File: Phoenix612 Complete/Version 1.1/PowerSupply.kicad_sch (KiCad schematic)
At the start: 20 parts, among them J2 PWR, J3 uC PTT, K1 G5V-2, Q1 2N3904, U3 LM7805

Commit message: Update 9Mar23
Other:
- moved on the sheet: C10
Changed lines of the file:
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@@
     (stroke (width 0) (type default) (color 0 0 0 0))
   )
-  (wire (pts (xy 51.435 102.235) (xy 51.435 103.505))
+  (wire (pts (xy 51.435 102.235) (xy 51.435 104.14))
     (stroke (width 0) (type default) (color 0 0 0 0))
   )
@@
     (stroke (width 0) (type default) (color 0 0 0 0))
   )
-  (wire (pts (xy 51.435 111.125) (xy 51.435 114.935))
+  (wire (pts (xy 51.435 111.76) (xy 51.435 114.935))
     (stroke (width 0) (type default) (color 0 0 0 0))
   )
@@
     (pin "2")
   )
-  (symbol (lib_id "Device:C_Polarized") (at 51.435 107.315 0) (unit 1)
-    (in_bom yes) (on_board yes) (fields_autoplaced)
-    (property "Reference" "C10" (id 0) (at 54.61 105.1559 0)
+  (symbol (lib_id "Device:C_Polarized") (at 51.435 107.95 0) (unit 1)
+    (in_bom yes) (on_board yes) (fields_autoplaced)
+    (property "Reference" "C10" (id 0) (at 54.61 105.7909 0)
       (effects (font (size 1.27 1.27)) (justify left))
     )
-    (property "Value" "22u" (id 1) (at 54.61 107.6959 0)
+    (property "Value" "22u" (id 1) (at 54.61 108.3309 0)
       (effects (font (size 1.27 1.27)) (justify left))
     )
-    (property "Footprint" "Capacitor_THT:CP_Radial_D8.0mm_P2.50mm" (id 2) (at 52.4002 111.125 0)
-      (effects (font (size 1.27 1.27)) hide)
-    )
-    (property "Datasheet" "~" (id 3) (at 51.435 107.315 0)
-      (effects (font (size 1.27 1.27)) hide)
-    )
+    (property "Footprint" "Capacitor_THT:CP_Radial_D8.0mm_P2.50mm" (id 2) (at 52.4002 111.76 0)
+      (effects (font (size 1.27 1.27)) hide)
+    )
+    (property "Datasheet" "~" (id 3) (at 51.435 107.95 0)
+      (effects (font (size 1.27 1.27)) hide)
+    )

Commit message: Update_17Mar23
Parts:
- added J51: VCC, Connector_BarrelJack:BarrelJack_GCT_DCJ200-10-A_Horizontal, symbol Connector:Barrel_Jack
- D1: value 1N4001 -> 1N5817; symbol Diode:1N4001 -> Diode:1N5817
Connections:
- net GND: now also J51.2
- net VCC: now reaches D1.2 (A), J2.2 (Pin_2)
- net VCC: now also J51.1
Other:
- moved on the sheet: D1, D2, D3, D4, R11, R12, R13

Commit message: Update 17Mar23
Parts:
- renumbered J2 to J3, J51 to J4, J3 to J5
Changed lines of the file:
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@@
   (symbol (lib_id "power:GND") (at 177.165 80.645 0) (unit 1)
     (in_bom yes) (on_board yes) (fields_autoplaced)
-    (property "Reference" "#PWR011" (id 0) (at 177.165 86.995 0)
+    (property "Reference" "#PWR022" (id 0) (at 177.165 86.995 0)
       (effects (font (size 1.27 1.27)) hide)
     )
@@
   (symbol (lib_id "Connector_Generic:Conn_01x03") (at 93.345 53.975 0) (unit 1)
     (in_bom yes) (on_board yes) (fields_autoplaced)
-    (property "Reference" "J2" (id 0) (at 96.52 52.7049 0)
+    (property "Reference" "J3" (id 0) (at 96.52 52.7049 0)
       (effects (font (size 1.27 1.27)) (justify left))
     )
@@
   (symbol (lib_id "Connector:Barrel_Jack") (at 55.245 55.245 0) (unit 1)
     (in_bom yes) (on_board yes) (fields_autoplaced)
-    (property "Reference" "J51" (id 0) (at 55.245 45.72 0))
+    (property "Reference" "J4" (id 0) (at 55.245 45.72 0))
     (property "Value" "VCC" (id 1) (at 55.245 48.26 0))
     (property "Footprint" "Connector_BarrelJack:BarrelJack_GCT_DCJ200-10-A_Horizontal" (id 2) (at 56.515 56.261 0)
@@
   (symbol (lib_id "power:PWR_FLAG") (at 78.105 33.02 180) (unit 1)
     (in_bom yes) (on_board yes)
-    (property "Reference" "#FLG016" (id 0) (at 78.105 34.925 0)
+    (property "Reference" "#FLG06" (id 0) (at 78.105 34.925 0)
       (effects (font (size 1.27 1.27)) hide)
     )
@@
   (symbol (lib_id "power:GND") (at 102.235 151.765 0) (unit 1)
     (in_bom yes) (on_board yes) (fields_autoplaced)
-    (property "Reference" "#PWR015" (id 0) (at 102.235 158.115 0)
+    (property "Reference" "#PWR026" (id 0) (at 102.235 158.115 0)
       (effects (font (size 1.27 1.27)) hide)
     )
@@
   (symbol (lib_id "power:GND") (at 33.655 32.385 0) (unit 1)
     (in_bom yes) (on_board yes) (fields_autoplaced)
-    (property "Reference" "#PWR09" (id 0) (at 33.655 38.735 0)
+    (property "Reference" "#PWR019" (id 0) (at 33.655 38.735 0)
       (effects (font (size 1.27 1.27)) hide)
     )
@@
   (symbol (lib_id "power:GND") (at 116.205 171.45 0) (unit 1)
     (in_bom yes) (on_board yes)
-    (property "Reference" "#PWR017" (id 0) (at 116.205 177.8 0)
+    (property "Reference" "#PWR028" (id 0) (at 116.205 177.8 0)
       (effects (font (size 1.27 1.27)) hide)
     )
@@
   (symbol (lib_id "power:GND") (at 66.675 57.785 0) (unit 1)
     (in_bom yes) (on_board yes) (fields_autoplaced)
-    (property "Reference" "#PWR010" (id 0) (at 66.675 64.135 0)
+    (property "Reference" "#PWR020" (id 0) (at 66.675 64.135 0)
       (effects (font (size 1.27 1.27)) hide)
     )
@@
   (symbol (lib_id "Connector_Generic:Conn_01x02") (at 121.285 165.1 0) (unit 1)
     (in_bom yes) (on_board yes) (fields_autoplaced)
-    (property "Reference" "J3" (id 0) (at 124.46 165.0999 0)
+    (property "Reference" "J5" (id 0) (at 124.46 165.0999 0)
       (effects (font (size 1.27 1.27)) (justify left))
     )
@@
   (symbol (lib_id "power:GND") (at 198.12 80.645 0) (unit 1)
     (in_bom yes) (on_board yes) (fields_autoplaced)
-    (property "Reference" "#PWR013" (id 0) (at 198.12 86.995 0)
+    (property "Reference" "#PWR024" (id 0) (at 198.12 86.995 0)
       (effects (font (size 1.27 1.27)) hide)
     )
@@
   (symbol (lib_id "power:GND") (at 134.62 154.94 0) (unit 1)
     (in_bom yes) (on_board yes) (fields_autoplaced)
-    (property "Reference" "#PWR016" (id 0) (at 134.62 161.29 0)
+    (property "Reference" "#PWR027" (id 0) (at 134.62 161.29 0)
       (effects (font (size 1.27 1.27)) hide)
     )
@@
   (symbol (lib_id "power:GND") (at 67.945 118.745 0) (unit 1)
     (in_bom yes) (on_board yes) (fields_autoplaced)
-    (property "Reference" "#PWR014" (id 0) (at 67.945 125.095 0)
+    (property "Reference" "#PWR025" (id 0) (at 67.945 125.095 0)
       (effects (font (size 1.27 1.27)) hide)
     )
@@
   (symbol (lib_id "power:GND") (at 81.28 59.055 0) (unit 1)
     (in_bom yes) (on_board yes) (fields_autoplaced)
-    (property "Reference" "#PWR0112" (id 0) (at 81.28 65.405 0)
+    (property "Reference" "#PWR021" (id 0) (at 81.28 65.405 0)
       (effects (font (size 1.27 1.27)) hide)
     )
@@
   (symbol (lib_id "power:GND") (at 187.325 80.645 0) (unit 1)
     (in_bom yes) (on_board yes) (fields_autoplaced)
-    (property "Reference" "#PWR012" (id 0) (at 187.325 86.995 0)
-      (effects (font (size 1.27 1.27)) hide)
-    )
+    (property "Reference" "#PWR023" (id 0) (at 187.325 86.995 0)
+      (effects (font (size 1.27 1.27)) hide)
+    )

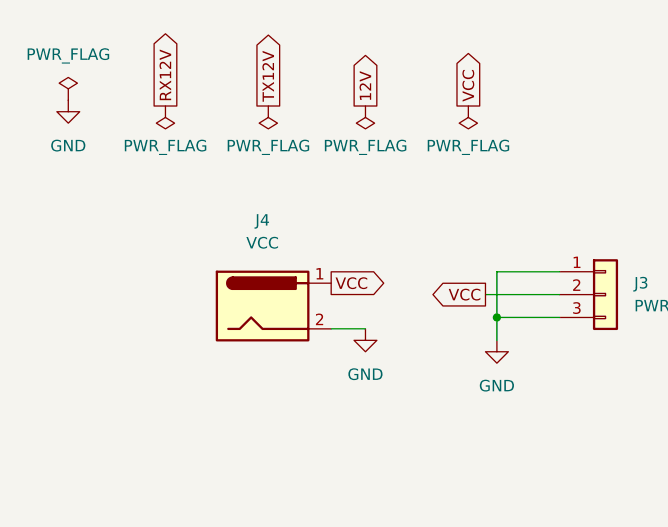
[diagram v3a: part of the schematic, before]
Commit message: Update LT1253 Tx
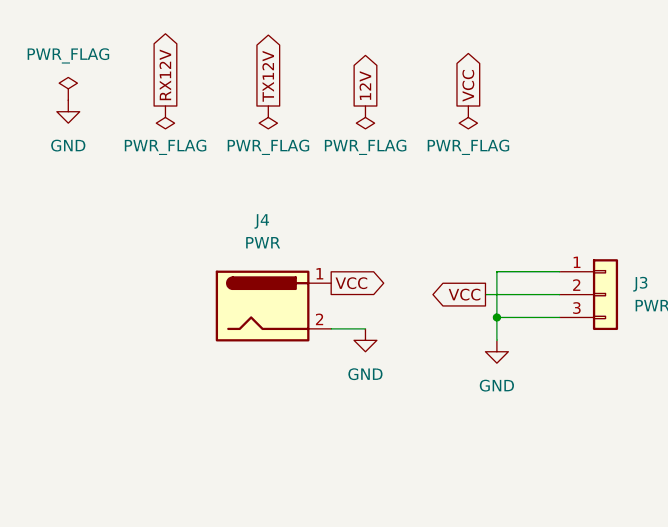
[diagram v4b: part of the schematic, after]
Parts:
- J4: value VCC -> PWR
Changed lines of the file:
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@@
     (in_bom yes) (on_board yes) (fields_autoplaced)
     (property "Reference" "J4" (id 0) (at 55.245 45.72 0))
-    (property "Value" "VCC" (id 1) (at 55.245 48.26 0))
+    (property "Value" "PWR" (id 1) (at 55.245 48.26 0))
     (property "Footprint" "Connector_BarrelJack:BarrelJack_GCT_DCJ200-10-A_Horizontal" (id 2) (at 56.515 56.261 0)
       (effects (font (size 1.27 1.27)) hide)

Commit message: Cleanup 8May23
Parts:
- C14: value 10n -> 22u
- R15: value 5K -> 4.7K
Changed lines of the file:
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@@
     (in_bom yes) (on_board yes) (fields_autoplaced)
     (property "Reference" "R15" (id 0) (at 123.19 143.51 90))
-    (property "Value" "5K" (id 1) (at 123.19 146.05 90))
+    (property "Value" "4.7K" (id 1) (at 123.19 146.05 90))
     (property "Footprint" "Resistor_SMD:R_1206_3216Metric" (id 2) (at 122.936 150.876 90)
       (effects (font (size 1.27 1.27)) hide)
@@
     (in_bom yes) (on_board yes) (fields_autoplaced)
     (property "Reference" "C14" (id 0) (at 108.585 142.24 90))
-    (property "Value" "10n" (id 1) (at 108.585 144.78 90))
+    (property "Value" "22u" (id 1) (at 108.585 144.78 90))
     (property "Footprint" "Capacitor_SMD:C_1206_3216Metric" (id 2) (at 112.395 148.8948 0)
       (effects (font (size 1.27 1.27)) hide)
